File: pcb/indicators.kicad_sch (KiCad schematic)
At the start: 8 parts

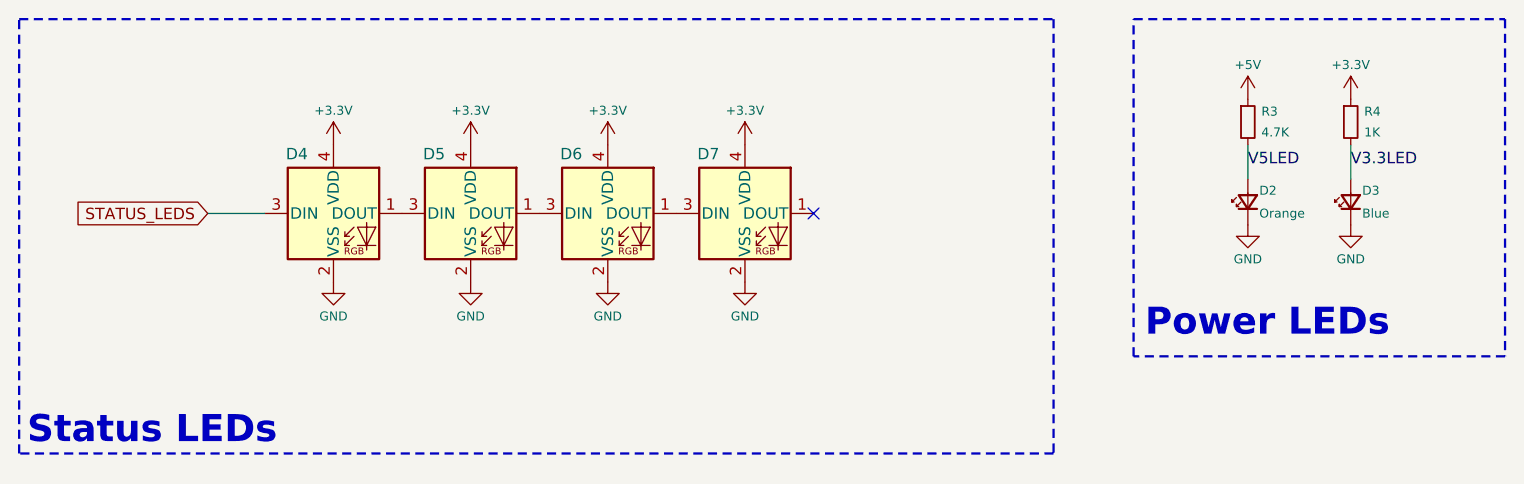
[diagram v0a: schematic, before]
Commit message: Updated license and implemented RP2040
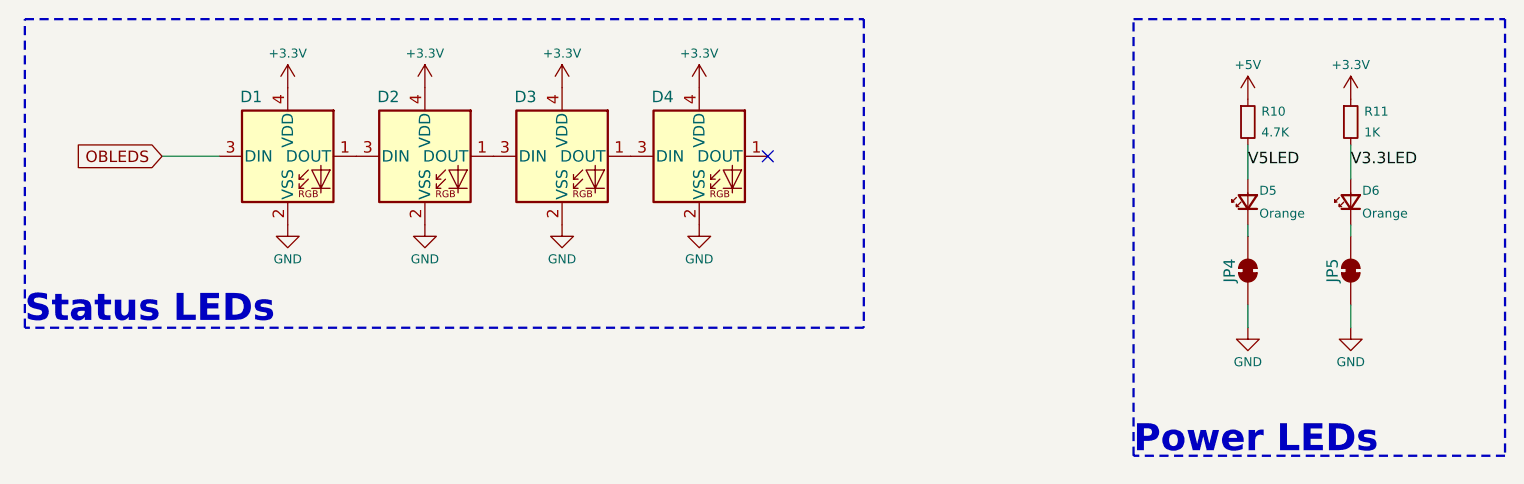
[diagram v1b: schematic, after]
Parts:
- removed D3: Blue, LED_SMD:LED_0603_1608Metric, symbol Device:LED_Small
- added D6: Orange, LED_SMD:LED_0603_1608Metric, symbol Device:LED_Small
- added JP4, JP5: ~, CRGM Connector:SolderJumper-2_P1.3mm_Bridged_RoundedPad1.0x1.5mm, symbol Jumper:SolderJumper_2_Bridged
- renumbered D4 to D1, D5 to D2, D6 to D3, D7 to D4, D2 to D5, R3 to R10, R4 to R11
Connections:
- net GND: now also JP4.1 (A), JP5.1 (A); no longer D5.1 (K)
- net V3.3LED: now also D6.2 (A)
- net STATUS_LEDS renamed OBLEDS
- new net: D5.1 (K), JP4.2 (B)
- new net: D6.1 (K), JP5.2 (B)
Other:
- moved on the sheet: D1, D2, D3, D4
